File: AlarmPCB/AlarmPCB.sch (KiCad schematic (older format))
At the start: 2 parts

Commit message: Addded LCD
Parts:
- removed U?: LTC-4727JR, symbol ECE:LTC-4727JR
- added DS?: WC1602A, Display:WC1602A, symbol Display_Character:WC1602A
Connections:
- net labels removed: Digit1, Digit2, Digit3, Digit4
- wire segments 12 -> 4
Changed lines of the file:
@@
 EESchema Schematic File Version 4
+LIBS:AlarmPCB-cache
 EELAYER 30 0
 EELAYER END
@@
 F 3 "https://www.arduino.cc/en/Main/arduinoBoardUno" H 2900 5050 50  0001 C CNN
 	1    3100 4000
-	1    0    0    -1
-$EndComp
-$Comp
-L ECE:LTC-4727JR U?
-U 1 1 5EFFC02F
-P 6450 3950
-F 0 "U?" H 6450 4587 60  0000 C CNN
-F 1 "LTC-4727JR" H 6450 4481 60  0000 C CNN
-F 2 "" H 5750 4350 60  0000 C CNN
-F 3 "" H 5750 4350 60  0000 C CNN
-	1    6450 3950
 	1    0    0    -1
 $EndComp
@@
 Wire Wire Line
 	3100 5100 3100 5250
-Wire Wire Line
-	2600 3700 2100 3700
-Wire Wire Line
-	2600 3900 2100 3900
-Wire Wire Line
-	2600 4000 2100 4000
-Wire Wire Line
-	2600 4300 2100 4300
-Wire Wire Line
-	5950 3600 5600 3600
-Wire Wire Line
-	5950 3700 5600 3700
-Wire Wire Line
-	5950 4100 5600 4100
-Wire Wire Line
-	5950 4300 5600 4300
-Text Label 2100 3700 0    50   ~ 0
-Digit1
-Text Label 2100 3900 0    50   ~ 0
-Digit2
-Text Label 2100 4000 0    50   ~ 0
-Digit3
-Text Label 2100 4300 0    50   ~ 0
-Digit4
-Text Label 5600 3600 0    50   ~ 0
-Digit1
-Text Label 5600 3700 0    50   ~ 0
-Digit2
-Text Label 5600 4100 0    50   ~ 0
-Digit3
-Text Label 5600 4300 0    50   ~ 0
-Digit4
+$Comp
+L Display_Character:WC1602A DS?
+U 1 1 5F063F5F
+P 5950 4050
+F 0 "DS?" H 5950 5031 50  0000 C CNN
+F 1 "WC1602A" H 5950 4940 50  0000 C CNN
+F 2 "Display:WC1602A" H 5950 3150 50  0001 C CIN
+F 3 "http://www.wincomlcd.com/pdf/WC1602A-SFYLYHTC06.pdf" H 6650 4050 50  0001 C CNN
+	1    5950 4050
+	1    0    0    -1
+$EndComp
 $EndSCHEMATC

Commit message: Added test
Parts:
- A?: symbol MCU_Module:Arduino_UNO_R3 -> AlarmPCB-rescue:Arduino_UNO_R3-MCU_Module
- gave numbers to parts that had none: 1
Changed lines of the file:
@@
 EESchema Schematic File Version 4
-LIBS:AlarmPCB-cache
 EELAYER 30 0
 EELAYER END
@@
 $EndDescr
 $Comp
-L MCU_Module:Arduino_UNO_R3 A?
+L AlarmPCB-rescue:Arduino_UNO_R3-MCU_Module A?
 U 1 1 5EFF97DB
 P 3100 4000
@@
 	3100 5100 3100 5250
 $Comp
-L Display_Character:WC1602A DS?
+L Display_Character:WC1602A Test
 U 1 1 5F063F5F
 P 5950 4050
-F 0 "DS?" H 5950 5031 50  0000 C CNN
+F 0 "Test" H 5950 5031 50  0000 C CNN
 F 1 "WC1602A" H 5950 4940 50  0000 C CNN
 F 2 "Display:WC1602A" H 5950 3150 50  0001 C CIN

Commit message: Added initial circuit layout
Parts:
- added BZ1: Buzzer, symbol Device:Buzzer
- added R1, R2: R_Small_US, symbol Device:R_Small_US
- added R3: R_PHOTO, symbol Device:R_PHOTO
- added RV1: R_POT, symbol Device:R_POT
- added SW1: TimeUp, symbol Switch:SW_Push
- added SW2: TimeDown, symbol Switch:SW_Push
- added SW4: AlarmSet, symbol Switch:SW_Push
- added SW5: CancelAlarm, symbol Switch:SW_Push
- added SW6: Snooze, symbol Switch:SW_Push
- added SW7: Backlight, symbol Switch:SW_Push
- A1: renamed from A?; symbol AlarmPCB-rescue:Arduino_UNO_R3-MCU_Module -> MCU_Module:Arduino_UNO_R3
- renumbered Test to DS1
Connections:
- net +5V: now also DS1.2 (VDD), R2.1, RV1.1
- net GND: now also DS1.1 (VSS), DS1.5 (R/W), BZ1.2 (+), R1.2, R3.2, RV1.3, SW1.2, SW2.2, SW4.2, SW5.2, SW6.2, SW7.2
- net CA: now reaches A1.10 (A1)
- net CA: now also SW5.1
- net Sn: now reaches A1.11 (A2)
- net Sn: now also SW6.1
- net BL: now reaches A1.12 (A3)
- net BL: now also SW7.1
- net AS: now reaches A1.13 (A4/SDA)
- net AS: now also SW4.1
- net D7: now reaches A1.17 (D2)
- net D7: now also DS1.14 (D7)
- net D6: now reaches A1.18 (D3)
- net D6: now also DS1.13 (D6)
- net D5: now reaches A1.19 (D4)
- net D5: now also DS1.12 (D5)
- net D4: now reaches A1.20 (D5)
- net D4: now also DS1.11 (D4)
- net T+: now reaches A1.21 (D6)
- net T+: now also SW1.1
- net T-: now reaches A1.22 (D7)
- net T-: now also SW2.1
- net Buz: now reaches A1.24 (D9)
- net Buz: now also BZ1.1 (-)
- net Backlight: now reaches A1.25 (D10)
- net Backlight: now also DS1.15 (LED(+))
- net E: now reaches A1.26 (D11)
- net E: now also DS1.6 (E)
- net RS: now reaches A1.27 (D12)
- net RS: now also DS1.4 (RS)
- net Light: now reaches A1.9 (A0)
- net Light: now also R2.2, R3.1
- net at DS1.16 (LED(-)): now also R1.1
- net at DS1.3 (VO): now also RV1.2
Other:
- note added: "Alarm Buzzer"
- note added: "Arduino"
- note added: "LCD Display"
- note added: "Light Sensor"
- note added: "User Buttons"
- moved on the sheet: A1, DS1

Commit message: Changed look of sch
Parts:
- A1: symbol MCU_Module:Arduino_UNO_R3 -> AlarmPCB-rescue:Arduino_UNO_R3-MCU_Module
- R3: value R_PHOTO -> Photoresistor
- RV1: value R_POT -> Contrast
- renumbered SW1 to PB1, SW2 to PB2, SW4 to PB4, SW5 to PB5, SW6 to PB6, SW7 to PB7
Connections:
- net 215: now reaches DS1.3 (VO), RV1.2
- net AS renamed 113
- net BL renamed 112
- net Backlight renamed 125
- net Buz renamed 124
- net CA renamed 110
- net D4 renamed 120
- net D5 renamed 119
- net D6 renamed 118
- net D7 renamed 117
- net Light renamed 109
- net Sn renamed 111
- net T+ renamed 121
- net T- renamed 122
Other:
- note removed: "Alarm Buzzer"
- note removed: "Light Sensor"
- note removed: "User Buttons"
- moved on the sheet: A1, DS1, PB1, PB2, PB4, PB5, PB6, PB7, R1, R2, R3

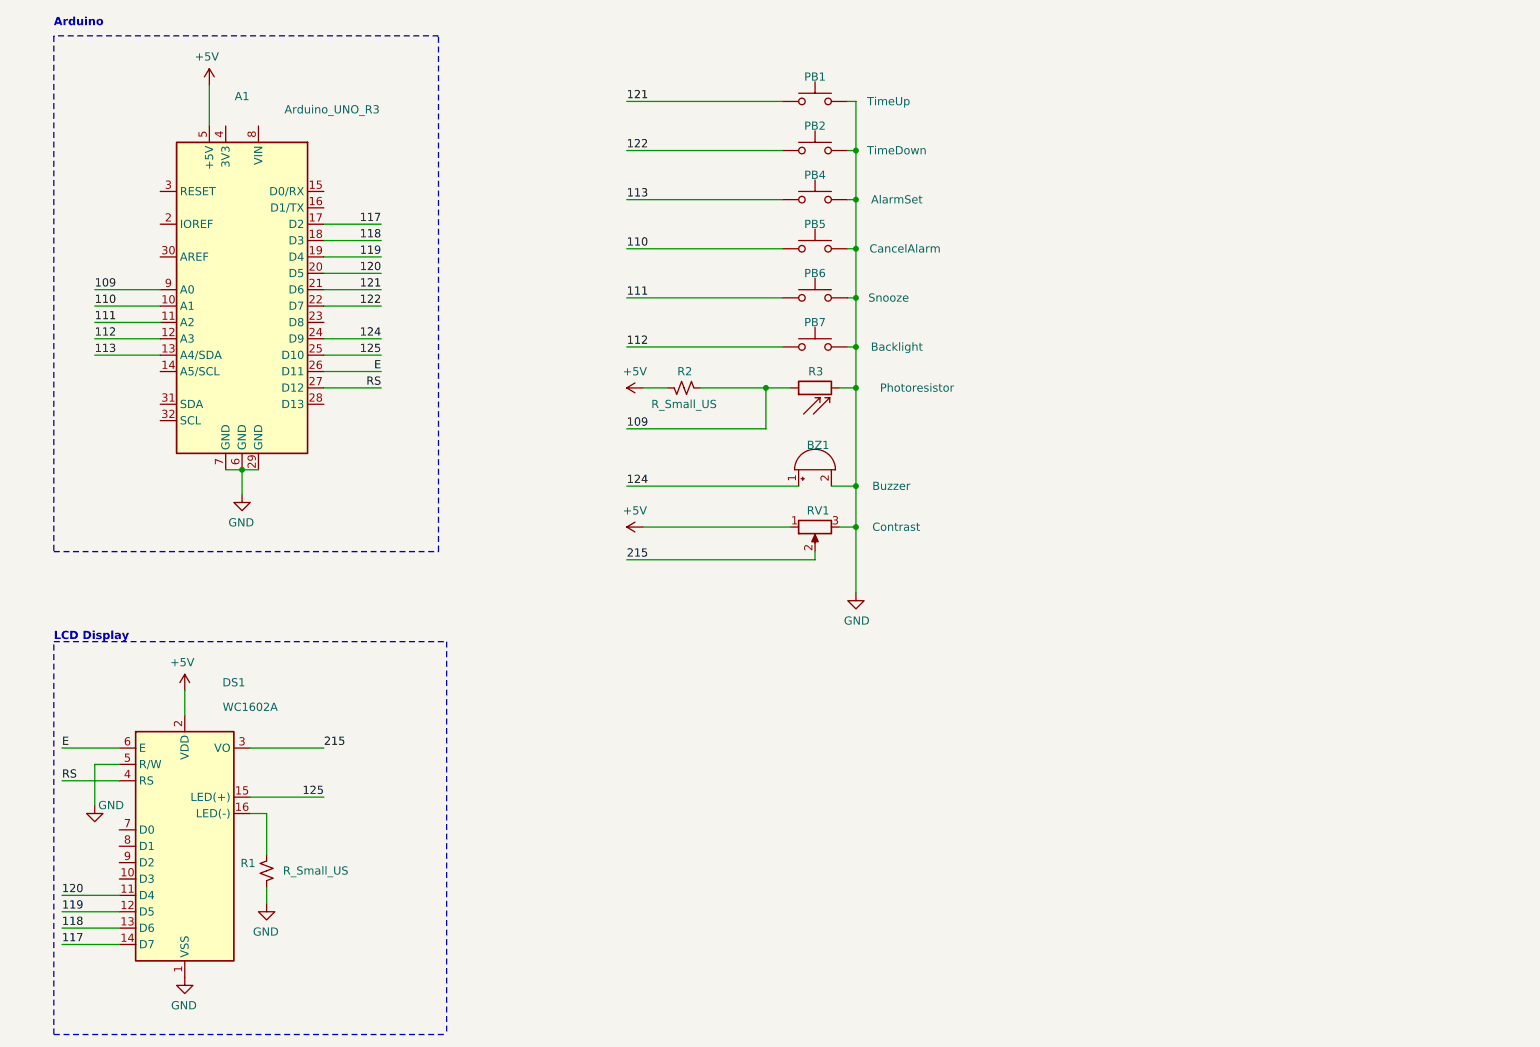
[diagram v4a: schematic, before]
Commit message: Cleaned up layout of sch
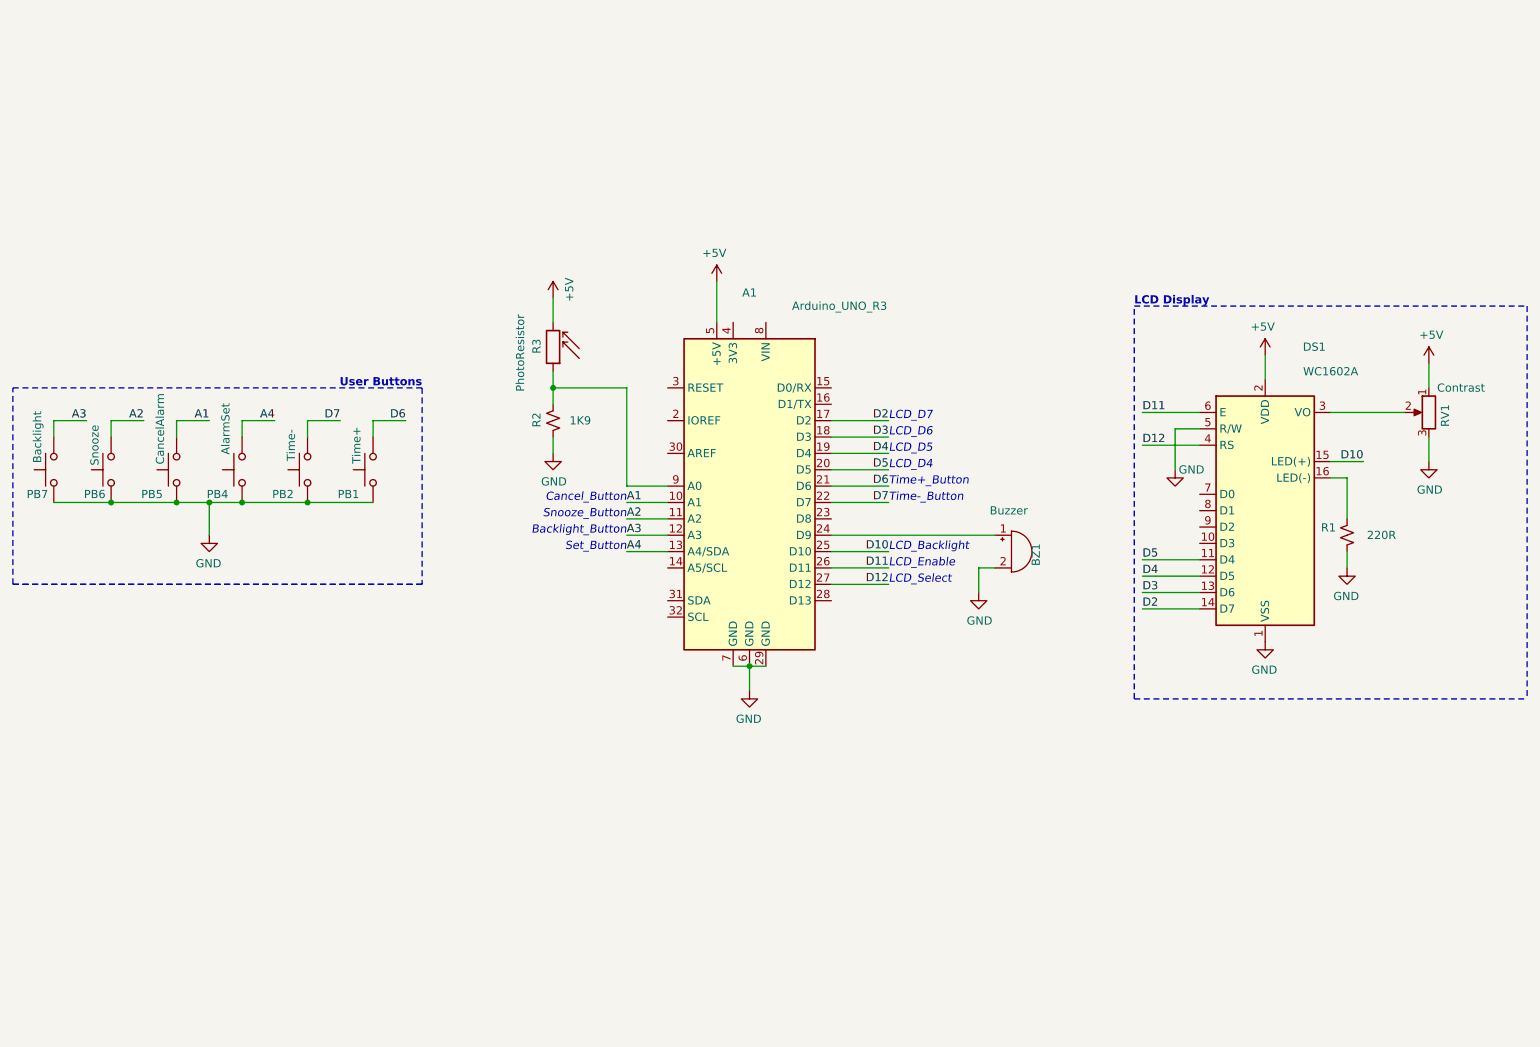
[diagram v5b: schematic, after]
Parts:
- PB1: value TimeUp -> Time+
- PB2: value TimeDown -> Time-
- R1: value R_Small_US -> 220R
- R2: value R_Small_US -> 1K9
- R3: value Photoresistor -> PhotoResistor
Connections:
- net +5V: now also R3.2; no longer R2.1
- net GND: now also R2.1; no longer R3.2
- net 109: no longer names the net of A1.9 (A0), R2.2, R3.1
- net 110 renamed A1
- net 111 renamed A2
- net 112 renamed A3
- net 113 renamed A4
- net 117 renamed D2
- net 118 renamed D3
- net 119 renamed D4
- net 120 renamed D5
- net 121 renamed D6
- net 122 renamed D7
- net 124: no longer names the net of A1.24 (D9), BZ1.1 (-)
- net 125 renamed D10
- net 215: no longer names the net of DS1.3 (VO), RV1.2
- net E renamed D11
- net RS renamed D12
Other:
- note added: "Backlight_Button"
- note added: "Cancel_Button"
- note added: "LCD_Backlight"
- note added: "LCD_D4"
- note added: "LCD_D5"
- note added: "LCD_D6"
- note added: "LCD_D7"
- note added: "LCD_Enable"
- note added: "LCD_Select"
- note added: "Set_Button"
- note added: "Snooze_Button"
- note added: "Time+_Button"
- note added: "Time-_Button"
- note added: "User Buttons"
- note removed: "Arduino"
- moved on the sheet: A1, BZ1, DS1, PB1, PB2, PB4, PB5, PB6, PB7, R1, R2, R3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

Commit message: Rough Draft
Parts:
- BZ1: footprint (none) -> Buzzer_Beeper:Buzzer_12x9.5RM7.6
- PB1, PB2, PB4, PB5, PB6, PB7: footprint (none) -> Button_Switch_THT:Push_E-Switch_KS01Q01
- R1, R2: footprint (none) -> Resistor_THT:R_Axial_DIN0309_L9.0mm_D3.2mm_P12.70mm_Horizontal
- R3: footprint (none) -> OptoDevice:R_LDR_4.9x4.2mm_P2.54mm_Vertical
- RV1: footprint (none) -> Potentiometer_THT:Potentiometer_ACP_CA6-H2,5_Horizontal
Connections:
- no-connect marks 0 -> 16
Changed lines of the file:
@@
 EESchema Schematic File Version 4
-LIBS:AlarmPCB-cache
 EELAYER 30 0
 EELAYER END
@@
 F 0 "R1" H 8968 4196 50  0000 L CNN
 F 1 "220R" H 8600 4150 50  0000 L CNN
-F 2 "" H 8900 4150 50  0001 C CNN
+F 2 "Resistor_THT:R_Axial_DIN0309_L9.0mm_D3.2mm_P12.70mm_Horizontal" H 8900 4150 50  0001 C CNN
 F 3 "~" H 8900 4150 50  0001 C CNN
 	1    8900 4150
@@
 F 0 "PB1" V 3100 3900 50  0000 C CNN
 F 1 "Time+" H 2800 3850 50  0000 C CNN
-F 2 "" H 2950 3950 50  0001 C CNN
+F 2 "Button_Switch_THT:Push_E-Switch_KS01Q01" H 2950 3950 50  0001 C CNN
 F 3 "~" H 2950 3950 50  0001 C CNN
 	1    2950 3750
@@
 F 0 "PB2" V 2700 3900 50  0000 C CNN
 F 1 "Time-" H 2400 3850 50  0000 C CNN
-F 2 "" H 2550 3950 50  0001 C CNN
+F 2 "Button_Switch_THT:Push_E-Switch_KS01Q01" H 2550 3950 50  0001 C CNN
 F 3 "~" H 2550 3950 50  0001 C CNN
 	1    2550 3750
@@
 F 0 "PB5" V 1900 3900 50  0000 C CNN
 F 1 "CancelAlarm" H 1500 3850 50  0000 C CNN
-F 2 "" H 1750 3950 50  0001 C CNN
+F 2 "Button_Switch_THT:Push_E-Switch_KS01Q01" H 1750 3950 50  0001 C CNN
 F 3 "~" H 1750 3950 50  0001 C CNN
 	1    1750 3750
@@
 F 0 "PB6" V 1500 3850 50  0000 C CNN
 F 1 "Snooze" H 1200 3850 50  0000 C CNN
-F 2 "" H 1350 3950 50  0001 C CNN
+F 2 "Button_Switch_THT:Push_E-Switch_KS01Q01" H 1350 3950 50  0001 C CNN
 F 3 "~" H 1350 3950 50  0001 C CNN
 	1    1350 3750
@@
 F 0 "PB7" V 1150 3850 50  0000 C CNN
 F 1 "Backlight" H 800 3850 50  0000 C CNN
-F 2 "" H 1000 3950 50  0001 C CNN
+F 2 "Button_Switch_THT:Push_E-Switch_KS01Q01" H 1000 3950 50  0001 C CNN
 F 3 "~" H 1000 3950 50  0001 C CNN
 	1    1000 3750
@@
 F 0 "BZ1" V 7000 4300 50  0000 R CNN
 F 1 "Buzzer" H 6950 4500 50  0000 R CNN
-F 2 "" V 6825 4350 50  0001 C CNN
+F 2 "Buzzer_Beeper:Buzzer_12x9.5RM7.6" V 6825 4350 50  0001 C CNN
 F 3 "~" V 6825 4350 50  0001 C CNN
 	1    6850 4250
@@
 F 0 "RV1" V 9300 3450 50  0000 R CNN
 F 1 "Contrast" H 9350 3550 50  0000 R CNN
-F 2 "" H 9400 3400 50  0001 C CNN
+F 2 "Potentiometer_THT:Potentiometer_ACP_CA6-H2,5_Horizontal" H 9400 3400 50  0001 C CNN
 F 3 "~" H 9400 3400 50  0001 C CNN
 	1    9400 3400
@@
 	9000 3700 8800 3700
 $Comp
-L power:GND #PWR?
+L power:GND #PWR0101
 U 1 1 5F0AF103
 P 9400 3700
-F 0 "#PWR?" H 9400 3450 50  0001 C CNN
+F 0 "#PWR0101" H 9400 3450 50  0001 C CNN
 F 1 "GND" H 9405 3527 50  0000 C CNN
 F 2 "" H 9400 3700 50  0001 C CNN
@@
 	9400 3700 9400 3550
 $Comp
-L power:+5V #PWR?
+L power:+5V #PWR0102
 U 1 1 5F0B0F52
 P 9400 3100
-F 0 "#PWR?" H 9400 2950 50  0001 C CNN
+F 0 "#PWR0102" H 9400 2950 50  0001 C CNN
 F 1 "+5V" H 9415 3273 50  0000 C CNN
 F 2 "" H 9400 3100 50  0001 C CNN
@@
 F 0 "R2" V 3950 3400 50  0000 L CNN
 F 1 "1K9" H 4150 3450 50  0000 L CNN
-F 2 "" H 4050 3450 50  0001 C CNN
+F 2 "Resistor_THT:R_Axial_DIN0309_L9.0mm_D3.2mm_P12.70mm_Horizontal" H 4050 3450 50  0001 C CNN
 F 3 "~" H 4050 3450 50  0001 C CNN
 	1    4050 3450
@@
 F 0 "R3" V 4150 2950 50  0000 L CNN
 F 1 "PhotoResistor" V 4250 2800 50  0000 L CNN
-F 2 "" V 4100 2750 50  0001 L CNN
+F 2 "OptoDevice:R_LDR_4.9x4.2mm_P2.54mm_Vertical" V 4100 2750 50  0001 L CNN
 F 3 "~" H 4050 2950 50  0001 C CNN
 	1    4050 3000
@@
 	4050 2700 4050 2850
 $Comp
-L power:GND #PWR?
+L power:GND #PWR0103
 U 1 1 5F0D1E03
 P 4050 3650
-F 0 "#PWR?" H 4050 3400 50  0001 C CNN
+F 0 "#PWR0103" H 4050 3400 50  0001 C CNN
 F 1 "GND" H 4055 3477 50  0000 C CNN
 F 2 "" H 4050 3650 50  0001 C CNN
@@
 F 0 "PB4" V 2300 3900 50  0000 C CNN
 F 1 "AlarmSet" H 1900 3850 50  0000 C CNN
-F 2 "" H 2150 3950 50  0001 C CNN
+F 2 "Button_Switch_THT:Push_E-Switch_KS01Q01" H 2150 3950 50  0001 C CNN
 F 3 "~" H 2150 3950 50  0001 C CNN
 	1    2150 3750
@@
 	1950 3950 2150 3950
 $Comp
-L power:GND #PWR?
+L power:GND #PWR0104
 U 1 1 5F1394E5
 P 1950 4150
-F 0 "#PWR?" H 1950 3900 50  0001 C CNN
+F 0 "#PWR0104" H 1950 3900 50  0001 C CNN
 F 1 "GND" H 1955 3977 50  0000 C CNN
 F 2 "" H 1950 4150 50  0001 C CNN
@@
 Wire Wire Line
 	4500 3250 4500 3850
+NoConn ~ 5150 2850
+NoConn ~ 5350 2850
+NoConn ~ 4750 3250
+NoConn ~ 4750 3450
+NoConn ~ 4750 3650
+NoConn ~ 4750 4350
+NoConn ~ 4750 4550
+NoConn ~ 4750 4650
+NoConn ~ 5750 4550
+NoConn ~ 5750 4050
+NoConn ~ 5750 3350
+NoConn ~ 5750 3250
+NoConn ~ 8000 3900
+NoConn ~ 8000 4000
+NoConn ~ 8000 4100
+NoConn ~ 8000 4200
 $EndSCHEMATC
